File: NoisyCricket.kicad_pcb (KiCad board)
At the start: 2 copper layers, 9 parts, among them J1 +9 V, J2 Audio-Jack-2_Switch, Q1 J201

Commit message: complete with elements
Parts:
- removed RV1: POT, Potentiometers:Potentiometer_Alps_RK09Y_Vertical
- added C2: 47n, Capacitors_THT:C_Disc_D7.5mm_W5.0mm_P10.00mm, F.Cu at (215.0, 133.3)
- added C3: 100mF, Capacitors_THT:CP_Radial_D13.0mm_P7.50mm, F.Cu at (197.2, 121.9)
- added C4: 100n, Capacitors_THT:C_Disc_D7.5mm_W5.0mm_P10.00mm, F.Cu at (236.8, 103.8)
- added C5: 100n, Capacitors_THT:C_Disc_D7.5mm_W5.0mm_P10.00mm, F.Cu at (189.8, 145.7)
- added C6: 100n, Capacitors_THT:C_Disc_D7.5mm_W5.0mm_P10.00mm, F.Cu at (222.5, 123.6)
- added C7: 47n, Capacitors_THT:C_Disc_D7.5mm_W5.0mm_P10.00mm, F.Cu at (202.8, 145.4)
- added C8: 220mF, Capacitors_THT:CP_Radial_D18.0mm_P7.50mm, F.Cu at (162.0, 110.3)
- added J3: +9 V, Pin_Headers:Pin_Header_Straight_1x02_Pitch2.00mm, F.Cu at (236.0, 121.8)
- added J4: Headphones plug, Pin_Headers:Pin_Header_Straight_1x03_Pitch2.00mm, F.Cu at (193.8, 133.8)
- added LS1: Speaker, Pin_Headers:Pin_Header_Straight_1x02_Pitch2.00mm, F.Cu at (229.6, 131.5)
- added R4: 10, Resistors_THT:R_Axial_DIN0614_L14.3mm_D5.7mm_P7.62mm_Vertical, F.Cu at (178.8, 148.8)
- added R5: 10, Resistors_THT:R_Axial_DIN0614_L14.3mm_D5.7mm_P7.62mm_Vertical, F.Cu at (225.7, 103.9)
- added SW1: SW_DIP_x01, Buttons_Switches_THT:SW_DIP_x1_W7.62mm_Slide_LowProfile, F.Cu at (236.6, 112.9)
- added U1: LM386, Housings_DIP:DIP-8_W7.62mm, F.Cu at (213.4, 102.4)
- added VR1: 10K, Potentiometers:Potentiometer_Alps_RK09Y_Vertical, F.Cu at (196.1, 108.5)
- added VR2: 1K, Potentiometers:Potentiometer_Alps_RK09Y_Vertical, F.Cu at (177.8, 122.6)
- added VR3: 100K, Potentiometers:Potentiometer_Alps_RK09Y_Vertical, F.Cu at (177.8, 108.5)
- C1: value C -> 220mF; footprint Capacitors_THT:C_Disc_D7.5mm_W5.0mm_P10.00mm -> Capacitors_THT:CP_Radial_D18.0mm_P7.50mm
- R1: value R -> 1M
- R2: value R -> 3K3
- R3: value R -> 4k7
- moved J1 79.6 mm to (250.4, 102.1)
- moved D1 78.2 mm to (246.9, 112.7)
- moved R1 48.2 mm to (225.7, 113.8)
- moved R2 38.0 mm to (203.9, 135.7), turned to 0 degrees
- moved J2 34.7 mm to (164.6, 147.4)
- moved C1 30.3 mm to (162.0, 133.0)
- moved R3 27.3 mm to (211.4, 118.3), turned to 0 degrees
- moved Q1 23.2 mm to (181.2, 135.2), turned to 0 degrees
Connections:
- C1 pad 2: Net-(C1-Pad2) -> GND
- D1 pad 1: GND -> Net-(D1-Pad1)
- Q1 pad 2: Net-(C1-Pad2) -> Net-(C2-Pad2)
- R2 pad 1: Net-(C1-Pad2) -> Net-(C2-Pad2)
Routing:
- net Net-(C1-Pad2): track 53.0 -> 0.00 mm
- net GND: track 45.6 -> 0.00 mm
- net Net-(J2-Pad1): track 21.5 -> 0.00 mm
- net Net-(D1-Pad2): track 19.0 -> 0.00 mm
- net Net-(J1-Pad1): track 13.8 -> 0.00 mm
- net Net-(C1-Pad1): track 5.08 -> 0.00 mm

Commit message: good for now
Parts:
- removed J1, J3: +9 V, Pin_Headers:Pin_Header_Straight_1x02_Pitch2.00mm
- removed J2: Audio-Jack-2_Switch, Pin_Headers:Pin_Header_Straight_1x03_Pitch2.00mm
- removed VR1: 10K, Potentiometers:Potentiometer_Alps_RK09Y_Vertical
- removed VR2: 1K, Potentiometers:Potentiometer_Alps_RK09Y_Vertical
- removed VR3: 100K, Potentiometers:Potentiometer_Alps_RK09Y_Vertical
- added BT1: Battery_Cell, Pin_Headers:Pin_Header_Straight_1x02_Pitch2.54mm, F.Cu at (171.4, 94.0)
- added GAIN1: 10k, DARKO:Pin_Header_Straight_1x03_Pitch2.54mm, F.Cu at (123.2, 118.1)
- added INPUT1: 10k, DARKO:Pin_Header_Straight_1x03_Pitch2.54mm, F.Cu at (170.2, 121.9)
- added TONE1: 10k, DARKO:Pin_Header_Straight_1x03_Pitch2.54mm, F.Cu at (153.7, 127.0)
- added input1: audio input, Pin_Headers:Pin_Header_Straight_1x03_Pitch2.00mm, F.Cu at (176.5, 121.9)
- C1, C8: footprint Capacitors_THT:CP_Radial_D18.0mm_P7.50mm -> Capacitors_THT:CP_Radial_D12.5mm_P2.50mm
- J4: value Headphones plug -> Headphones
- R1, R2, R3, R4, R5: footprint Resistors_THT:R_Axial_DIN0614_L14.3mm_D5.7mm_P7.62mm_Vertical -> Resistors_THT:R_Axial_DIN0411_L9.9mm_D3.6mm_P7.62mm_Vertical
- moved D1 102.2 mm to (146.1, 96.5)
- moved R5 93.7 mm to (134.6, 125.7), turned to 90 degrees
- moved C4 89.7 mm to (148.6, 87.6)
- moved C3 75.3 mm to (128.3, 91.4), turned to 180 degrees
- moved R3 75.0 mm to (143.5, 86.4), turned to 180 degrees
- moved J4 72.7 mm to (121.9, 123.2), turned to 90 degrees
- moved C7 72.2 mm to (143.5, 104.1), turned to 180 degrees
- moved SW1 71.1 mm to (170.2, 87.6), turned to 180 degrees
- moved LS1 67.2 mm to (162.6, 127.0), turned to 90 degrees
- moved R1 64.3 mm to (162.6, 101.6)
- moved R2 62.7 mm to (154.9, 96.5)
- moved Q1 59.5 mm to (137.2, 95.2), turned to 270 degrees
- moved R4 58.5 mm to (134.6, 110.5)
- moved C6 57.4 mm to (165.1, 120.7), turned to 180 degrees
- moved C5 57.2 mm to (139.7, 118.1)
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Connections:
- C1 pad 1: Net-(C1-Pad1) -> Net-(BT1-Pad1)
- C8 pad 1: Net-(C8-Pad1) -> Net-(C4-Pad1)
- D1 pad 1: Net-(D1-Pad1) -> GND
- Q1 pad 1: Net-(J1-Pad1) -> Net-(BT1-Pad1)
- R3 pad 2: Net-(J1-Pad1) -> Net-(BT1-Pad1)
- R4 pad 1: Net-(R4-Pad1) -> Net-(C4-Pad1)
- SW1 pad 1: Net-(SW1-Pad1) -> Net-(C3-Pad1)
- U1 pad 5: Net-(C8-Pad1) -> Net-(C4-Pad1)
- U1 pad 6: Net-(C1-Pad1) -> Net-(BT1-Pad1)
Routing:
- net GND: track 0.00 -> 148.2 mm
- net Net-(C4-Pad1): track 0.00 -> 91.6 mm
- net Net-(BT1-Pad1): track 0.00 -> 79.8 mm
- net Net-(GAIN1-Pad2): track 0.00 -> 65.0 mm
- net Net-(C3-Pad1): track 0.00 -> 63.3 mm
- net Net-(GAIN1-Pad1): track 0.00 -> 60.6 mm
- net Net-(Q1-Pad3): track 0.00 -> 53.3 mm
- net Net-(J4-Pad3): track 0.00 -> 38.2 mm
- net Net-(C2-Pad2): track 0.00 -> 37.8 mm
- net Net-(C8-Pad2): track 0.00 -> 29.6 mm
- net Net-(C6-Pad1): track 0.00 -> 23.4 mm
- net Net-(C6-Pad2): track 0.00 -> 22.1 mm
- net Net-(D1-Pad2): track 0.00 -> 12.3 mm
- net Net-(C5-Pad2): track 0.00 -> 11.9 mm
- net Net-(C7-Pad2): track 0.00 -> 11.4 mm
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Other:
- net class Default: trace_width 0.25 -> 0.5

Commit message: one layer
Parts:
- moved BT1 96.8 mm to (78.7, 121.9), turned to 180 degrees
- moved C2 92.9 mm to (78.7, 100.3)
- moved INPUT1 92.7 mm to (78.7, 106.7)
- moved input1 87.3 mm to (95.2, 90.2), turned to 270 degrees
- moved U1 74.4 mm to (101.6, 109.2), turned to 90 degrees
- moved R1 72.2 mm to (91.4, 114.3), turned to 180 degrees
- moved R2 70.0 mm to (85.1, 91.4), turned to 270 degrees
- moved TONE1 65.0 mm to (88.9, 121.9)
- moved C6 62.2 mm to (102.9, 120.7)
- moved SW1 48.7 mm to (123.2, 100.3), turned to 0 degrees
- moved D1 46.2 mm to (100.3, 90.2)
- moved Q1 45.9 mm to (92.7, 106.7)
- moved R3 45.9 mm to (99.1, 97.8)
- moved C5 42.1 mm to (97.8, 114.3)
- moved C1 41.8 mm to (111.8, 94.0)
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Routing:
- net GND: track 148.2 -> 0.00 mm
- net Net-(C4-Pad1): track 91.6 -> 0.00 mm
- net Net-(BT1-Pad1): track 79.8 -> 0.00 mm
- net Net-(GAIN1-Pad2): track 65.0 -> 0.00 mm
- net Net-(C3-Pad1): track 63.3 -> 0.00 mm
- net Net-(GAIN1-Pad1): track 60.6 -> 0.00 mm
- net Net-(Q1-Pad3): track 53.3 -> 0.00 mm
- net Net-(J4-Pad3): track 38.2 -> 0.00 mm
- net Net-(C2-Pad2): track 37.8 -> 0.00 mm
- net Net-(C8-Pad2): track 29.6 -> 0.00 mm
- net Net-(C6-Pad1): track 23.4 -> 0.00 mm
- net Net-(C6-Pad2): track 22.1 -> 0.00 mm
- net Net-(D1-Pad2): track 12.3 -> 0.00 mm
- net Net-(C5-Pad2): track 11.9 -> 0.00 mm
- net Net-(C7-Pad2): track 11.4 -> 0.00 mm
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
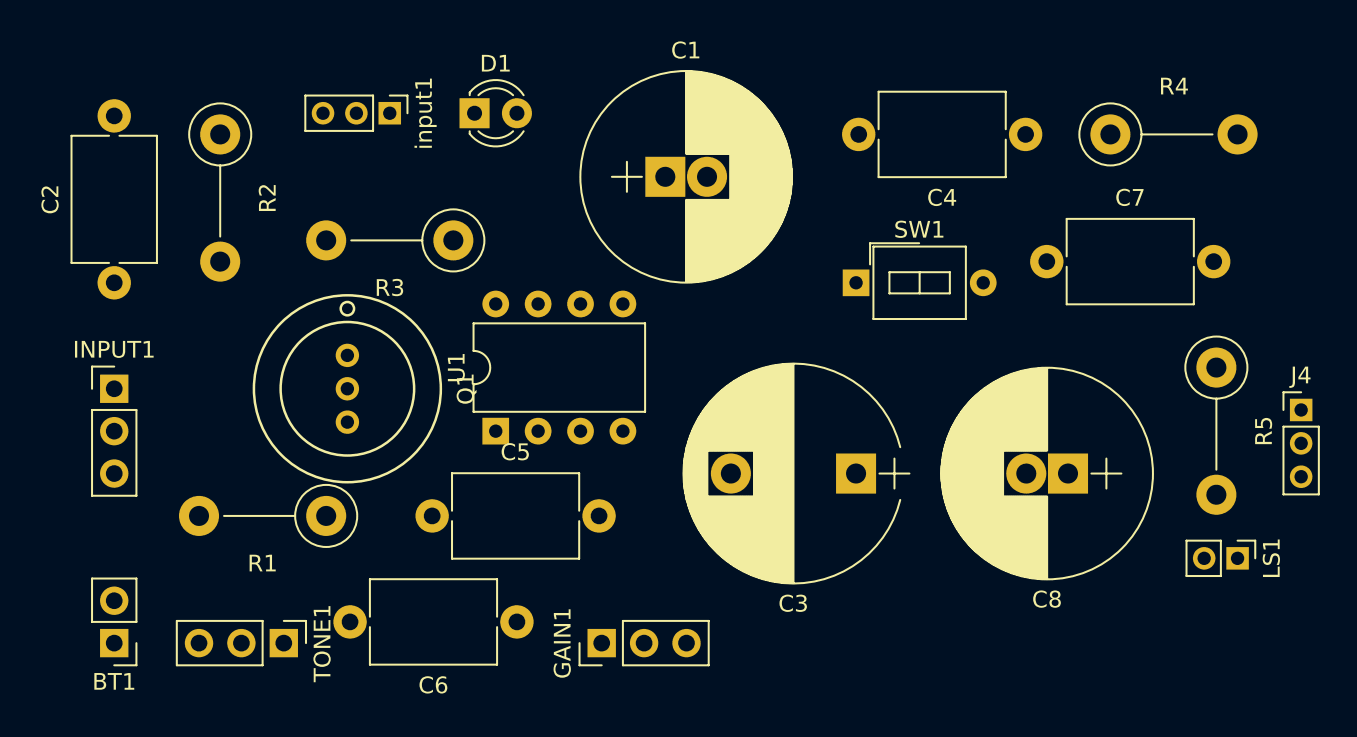
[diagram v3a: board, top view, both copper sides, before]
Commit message: comonents little closer
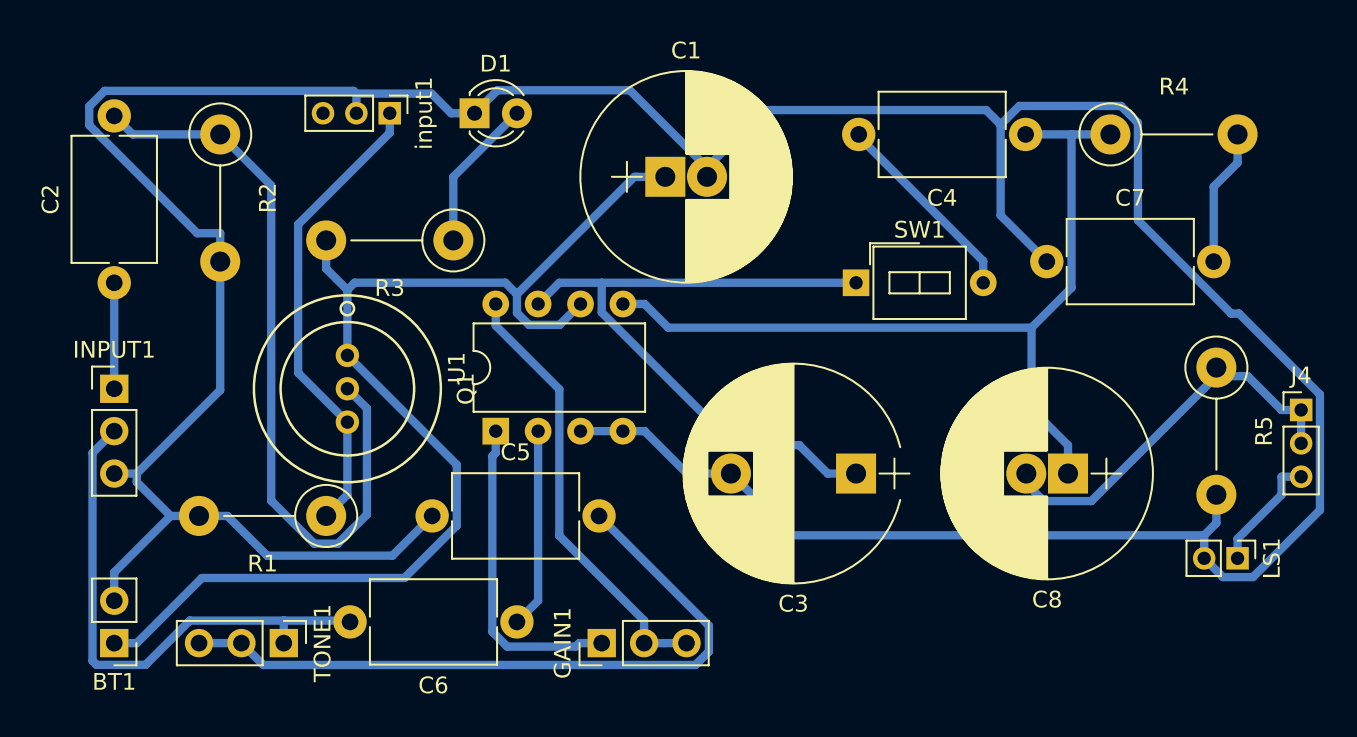
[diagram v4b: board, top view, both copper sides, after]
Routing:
- net GND: track 0.00 -> 218.1 mm
- net Net-(BT1-Pad1): track 0.00 -> 71.9 mm
- net Net-(C4-Pad1): track 0.00 -> 52.4 mm
- net Net-(C2-Pad2): track 0.00 -> 45.6 mm
- net Net-(C5-Pad2): track 0.00 -> 42.3 mm
- net Net-(C3-Pad1): track 0.00 -> 40.6 mm
- net Net-(C6-Pad2): track 0.00 -> 32.3 mm
- net Net-(Q1-Pad3): track 0.00 -> 28.2 mm
- net Net-(GAIN1-Pad2): track 0.00 -> 26.5 mm
- net Net-(C8-Pad2): track 0.00 -> 24.0 mm
- net Net-(GAIN1-Pad1): track 0.00 -> 19.1 mm
- net Net-(C4-Pad2): track 0.00 -> 12.0 mm
- net Net-(C6-Pad1): track 0.00 -> 12.0 mm
- net Net-(D1-Pad2): track 0.00 -> 9.20 mm
- net Net-(C7-Pad2): track 0.00 -> 8.21 mm
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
